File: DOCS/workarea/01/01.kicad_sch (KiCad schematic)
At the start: 12 parts

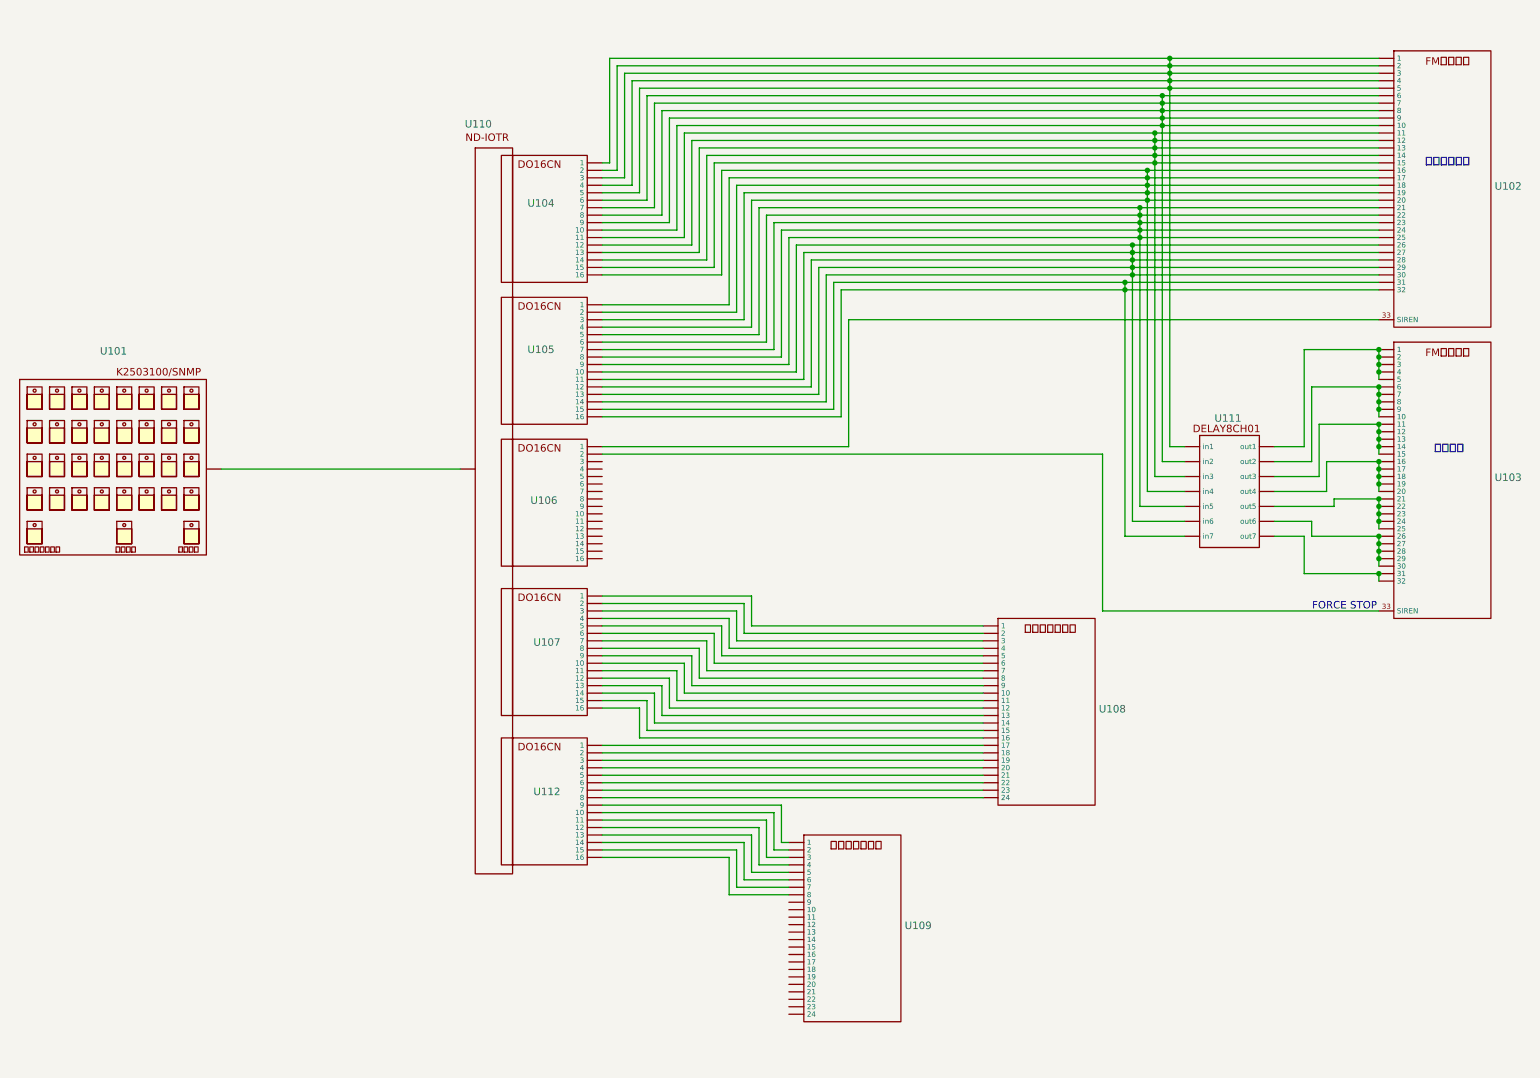
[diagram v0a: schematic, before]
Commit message: 説明文書構成図で遅延装置無し版を作成DIAGRAM02.pdf
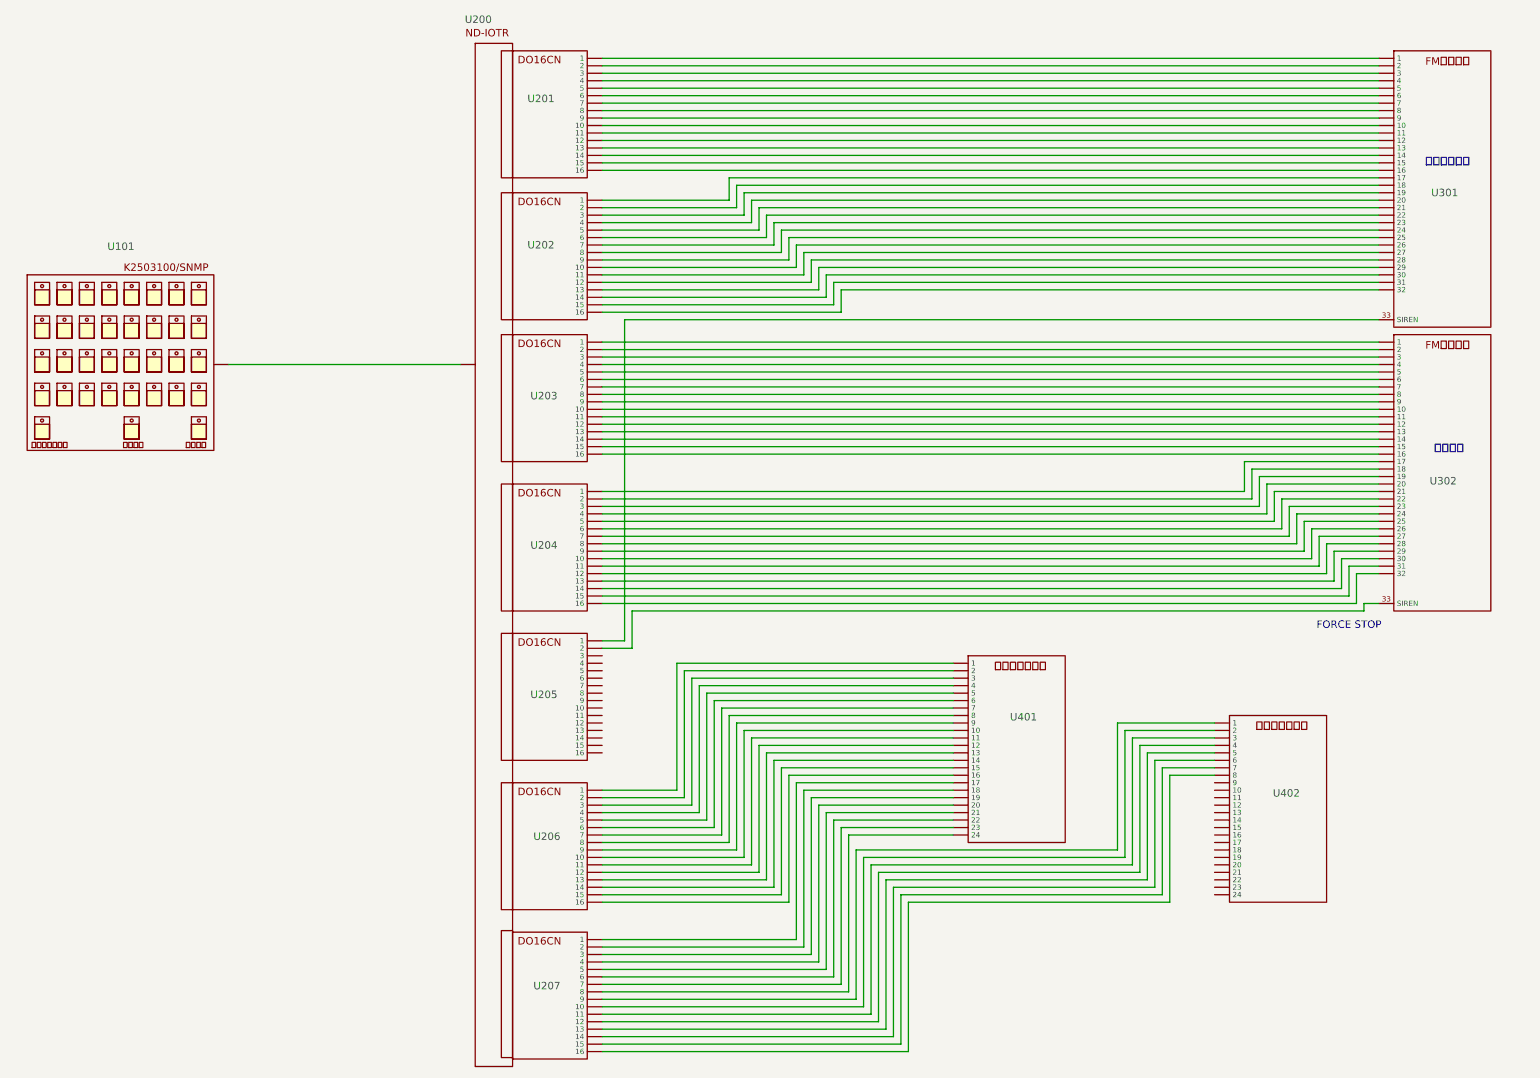
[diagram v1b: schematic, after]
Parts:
- removed U111: ~, symbol K2503100:DELAY8CH01
- added U203, U204: ~, symbol K2503100:DO16CN
- renumbered U110 to U200, U104 to U201, U105 to U202, U106 to U205, U107 to U206, U112 to U207, U102 to U301, U103 to U302, U108 to U401, U109 to U402
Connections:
- net at U301. (9): now also U202. (9); no longer U201. (9)
- net at U302. (9): now also U203. (9)
- net at U207. (9): now also U401. (9); no longer U402. (9)
- net at U402. (9): no longer U207. (9)
- net at U401. (9): now also U206. (9); no longer U207. (9)
- net at U205. (9): now also U302.33 (SIREN)
- new net: U204. (9), U302. (9) (x16)
- new net: U207. (9), U402. (9) (x8)
- new net: U207. (9), U401. (9) (x7)
- new net: U206. (9), U401. (9) (x15)
- new net: U201. (9), U301. (9) (x15)
- new net: U202. (9), U301. (9) (x15)
- new net: U203. (9), U302. (9) (x15)
- now unconnected: U402. (9), U402. (9), U402. (9), U402. (9), U402. (9), U402. (9)
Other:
- moved on the sheet: U101, U201, U202, U205, U206, U207, U302, U401, U402
